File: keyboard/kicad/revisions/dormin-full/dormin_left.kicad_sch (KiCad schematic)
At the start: 104 parts, among them J6_R1 Conn_01x04, Q3_R1 AO3407A, Q4_R1 AO3400A, SW21 SW_Push, SW22 SW_Push, SW23 SW_Push, SW24 SW_Push, SW25 SW_Push, SW26 SW_Push, SW27 SW_Push, SW28 SW_Push, SW29 SW_Push, SW30 SW_Push, SW31 SW_Push, SW32 SW_Push, SW33 SW_Push, SW34 SW_Push, SW35 SW_Push, SW36 SW_Push, SW37 SW_Push, SW38 SW_Push, SW39 SW_Push, SW40 SW_Push, U2 Seeeduino Xiao nRF52840

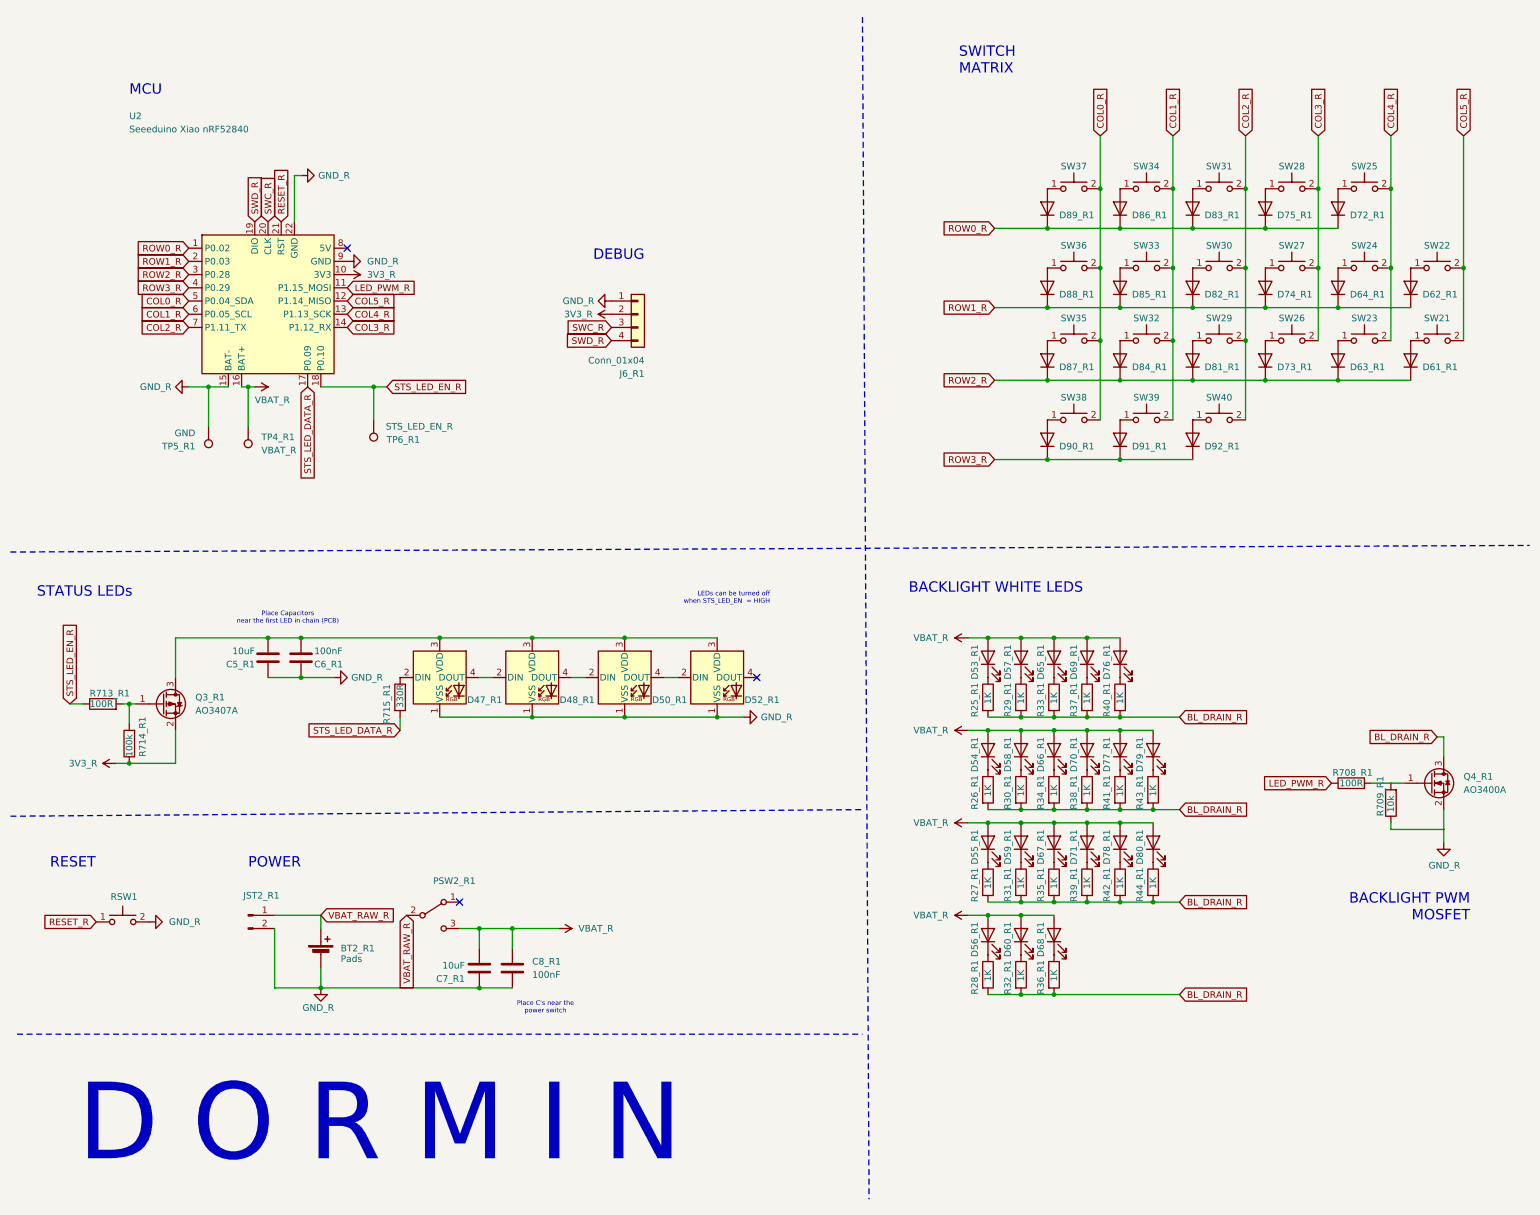
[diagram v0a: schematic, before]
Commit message: feat: remove unused components for v1
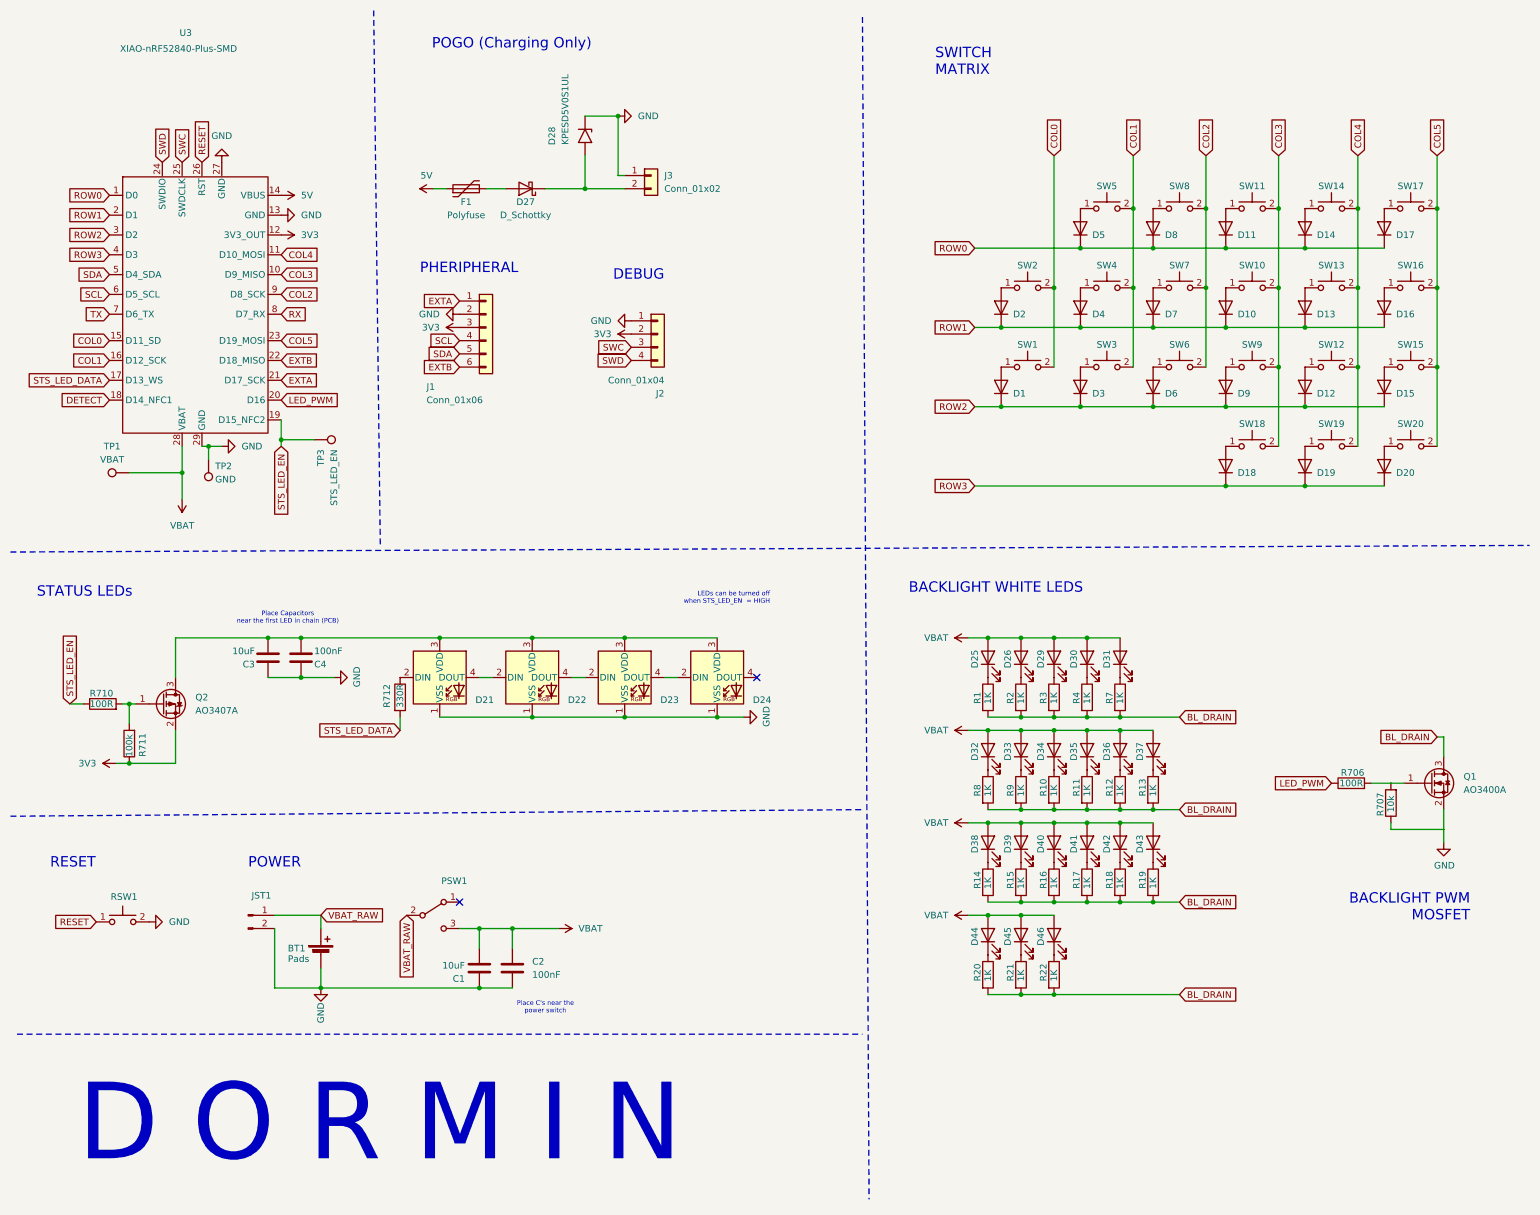
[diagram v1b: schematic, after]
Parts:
- removed BT2_R1: Pads, willkeebs_power:Battery_Pad, symbol Device:Battery_Cell
- removed C5_R1, C7_R1: 10uF, Capacitor_SMD:C_0603_1608Metric, symbol Device:C
- removed C6_R1, C8_R1: 100nF, Capacitor_SMD:C_0603_1608Metric, symbol Device:C
- removed D47_R1, D48_R1, D50_R1, D52_R1: SK6812MINI-E, LED_SMD:LED_SK6812MINI-E_3.2x2.8mm_P1.5mm_ReverseMount, symbol LED:SK6812MINI-E
- removed D53_R1, D54_R1, D55_R1, D56_R1, D57_R1, D58_R1, D59_R1, D60_R1, D65_R1, D66_R1, D67_R1, D68_R1, D69_R1, D70_R1, D71_R1, D76_R1, D77_R1, D78_R1, D79_R1, D80_R1: LED, willkeebs_components:LED_MHT151WDT, symbol Device:LED
- removed D61_R1, D62_R1, D63_R1, D64_R1, D72_R1, D73_R1, D74_R1, D75_R1, D81_R1, D82_R1, D83_R1, D84_R1, D85_R1, D86_R1, D87_R1, D88_R1, D89_R1, D90_R1, D91_R1, D92_R1: 1N4148W, Diode_SMD:D_SOD-123, symbol Diode:1N4148W
- removed J6_R1: Conn_01x04, Connector_PinSocket_2.54mm:PinSocket_1x04_P2.54mm_Vertical, symbol Connector_Generic:Conn_01x04
- removed JST2_R1: Conn_01x02_Pin, Connector_JST:JST_GH_SM02B-GHS-TB_1x02-1MP_P1.25mm_Horizontal, symbol Connector:Conn_01x02_Pin
- removed PSW2_R1: SW_SPDT, PCM_marbastlib-various:SW_MSK12C02-HB, symbol Switch:SW_SPDT
- removed Q3_R1: AO3407A, Package_TO_SOT_SMD:SOT-23, symbol Transistor_FET:AO3401A
- removed Q4_R1: AO3400A, Package_TO_SOT_SMD:SOT-23, symbol Transistor_FET:AO3400A
- removed R25_R1, R26_R1, R27_R1, R28_R1, R29_R1, R30_R1, R31_R1, R32_R1, R33_R1, R34_R1, R35_R1, R36_R1, R37_R1, R38_R1, R39_R1, R40_R1, R41_R1, R42_R1, R43_R1, R44_R1: 1K, Resistor_SMD:R_0603_1608Metric, symbol Device:R
- removed R708_R1, R713_R1: 100R, Resistor_SMD:R_0603_1608Metric, symbol Device:R
- removed R709_R1: 10k, Resistor_SMD:R_0603_1608Metric, symbol Device:R
- removed R714_R1: 100k, Resistor_SMD:R_0603_1608Metric, symbol Device:R
- removed R715_R1: 330R, Resistor_SMD:R_0603_1608Metric, symbol Device:R
- removed RSW2_R1: RSW1, Button_Switch_SMD:SW_SPST_SKQG_WithStem, symbol Switch:SW_Push
- removed SW21, SW22, SW23, SW24, SW25, SW26, SW27, SW28, SW29, SW30, SW31, SW32, SW33, SW34, SW35, SW36, SW37, SW38, SW39, SW40: SW_Push, willkeebs_keyboard:NF_LED_1206_SW_KS33_3_0_HS_1U, symbol Switch:SW_Push
- removed TP4_R1: VBAT_R, TestPoint:TestPoint_Pad_D1.0mm, symbol Connector:TestPoint
- removed TP5_R1: GND, TestPoint:TestPoint_Pad_D1.0mm, symbol Connector:TestPoint
- removed TP6_R1: STS_LED_EN_R, TestPoint:TestPoint_Pad_D1.0mm, symbol Connector:TestPoint
- removed U2: Seeeduino Xiao nRF52840, Seeed_Studio_XIAO_Series:XIAO-nRF52840-SMD, symbol PCM_marbastlib-promicroish:Seeeduino_Xiao_nRF52840
- added BT1: Pads, willkeebs_power:Battery_Pad, symbol Device:Battery_Cell
- added C1, C3: 10uF, Capacitor_SMD:C_0603_1608Metric, symbol Device:C
- added C2, C4: 100nF, Capacitor_SMD:C_0603_1608Metric, symbol Device:C
- added D1, D10, D11, D12, D13, D14, D15, D16, D17, D18, D19, D2, D20, D3, D4, D5, D6, D7, D8, D9: 1N4148W, Diode_SMD:D_SOD-123, symbol Diode:1N4148W
- added D21, D22, D23, D24: SK6812MINI-E, LED_SMD:LED_SK6812MINI-E_3.2x2.8mm_P1.5mm_ReverseMount, symbol LED:SK6812MINI-E
- added D25, D26, D29, D30, D31, D32, D33, D34, D35, D36, D37, D38, D39, D40, D41, D42, D43, D44, D45, D46: LED, willkeebs_components:LED_MHT151WDT, symbol Device:LED
- added D27: D_Schottky, Diode_SMD:D_SOD-523, symbol Device:D_Schottky
- added D28: KPESD5V0S1UL, Diode_SMD:D_SOD-882, symbol Diode:SMF5V0A
- added F1: Polyfuse, Fuse:Fuse_1206_3216Metric, symbol Device:Polyfuse
- added J1: Conn_01x06, willkeebs_misc:SMD_Conn_1x06_P2.54mm_Vertical, symbol Connector_Generic:Conn_01x06
- added J2: Conn_01x04, Connector_PinSocket_2.54mm:PinSocket_1x04_P2.54mm_Vertical, symbol Connector_Generic:Conn_01x04
- added J3: Conn_01x02, willkeebs_components:Pogo1x2-Right-Angle, symbol Connector_Generic:Conn_01x02
- added JST1: Conn_01x02_Pin, Connector_JST:JST_GH_SM02B-GHS-TB_1x02-1MP_P1.25mm_Horizontal, symbol Connector:Conn_01x02_Pin
- added PSW1: SW_SPDT, PCM_marbastlib-various:SW_MSK12C02-HB, symbol Switch:SW_SPDT
- added Q1: AO3400A, Package_TO_SOT_SMD:SOT-23, symbol Transistor_FET:AO3400A
- added Q2: AO3407A, Package_TO_SOT_SMD:SOT-23, symbol Transistor_FET:AO3401A
- added R1, R10, R11, R12, R13, R14, R15, R16, R17, R18, R19, R2, R20, R21, R22, R3, R4, R7, R8, R9: 1K, Resistor_SMD:R_0603_1608Metric, symbol Device:R
- added R706, R710: 100R, Resistor_SMD:R_0603_1608Metric, symbol Device:R
- added R707: 10k, Resistor_SMD:R_0603_1608Metric, symbol Device:R
- added R711: 100k, Resistor_SMD:R_0603_1608Metric, symbol Device:R
- added R712: 330R, Resistor_SMD:R_0603_1608Metric, symbol Device:R
- added RSW1: RSW1, Button_Switch_SMD:SW_SPST_SKQG_WithStem, symbol Switch:SW_Push
- added SW1, SW10, SW11, SW12, SW13, SW14, SW15, SW16, SW17, SW18, SW19, SW2, SW20, SW3, SW4, SW5, SW6, SW7, SW8, SW9: SW_Push, willkeebs_keyboard:NF_LED_1206_SW_KS33_3_0_HS_1U, symbol Switch:SW_Push
- added TP1: VBAT, TestPoint:TestPoint_Pad_D1.0mm, symbol Connector:TestPoint
- added TP2: GND, TestPoint:TestPoint_Pad_D1.0mm, symbol Connector:TestPoint
- added TP3: STS_LED_EN, TestPoint:TestPoint_Pad_D1.0mm, symbol Connector:TestPoint
- added U3: XIAO-nRF52840-Plus-SMD, Seeed_Studio_XIAO_Series:XIAO-nRF52840-Plus-SMD, symbol Seeed_Studio_XIAO_Series:XIAO-nRF52840_Plus_SMD
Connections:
- new net: D39.1 (K), R15.1
- new net: D32.1 (K), R8.1
- new net: D38.1 (K), R14.1
- new net: D20.2 (A), SW20.1
- new net: D43.1 (K), R19.1
- new net: D21.2 (DIN), R712.1
- new net: C3.2, C4.1, D21.3 (VDD), D22.3 (VDD), D23.3 (VDD), D24.3 (VDD), Q2.3 (D)
- new net: D2.2 (A), SW2.1
- new net: D19.2 (A), SW19.1
- new net: D35.1 (K), R11.1
- new net: D45.1 (K), R21.1
- new net: D9.2 (A), SW9.1
- new net: D14.2 (A), SW14.1
- new net: D33.1 (K), R9.1
- new net: D27.1 (K), D28.2 (A2), J3.2 (Pin_2)
- new net: D3.2 (A), SW3.1
- new net: D5.2 (A), SW5.1
- new net: D37.1 (K), R13.1
- new net: D4.2 (A), SW4.1
- new net: D11.2 (A), SW11.1
- new net: D13.2 (A), SW13.1
- new net: D12.2 (A), SW12.1
- new net: D31.1 (K), R7.1
- new net: D26.1 (K), R2.1
- new net: D6.2 (A), SW6.1
- new net: D27.2 (A), F1.2
- new net: D40.1 (K), R16.1
- new net: Q2.1 (G), R710.2, R711.2
- new net: D15.2 (A), SW15.1
- new net: D21.4 (DOUT), D22.2 (DIN)
- new net: D22.4 (DOUT), D23.2 (DIN)
- new net: D23.4 (DOUT), D24.2 (DIN)
- new net: D8.2 (A), SW8.1
- new net: D18.2 (A), SW18.1
- new net: D1.2 (A), SW1.1
- new net: D41.1 (K), R17.1
- new net: Q1.1 (G), R706.2, R707.2
- new net: D36.1 (K), R12.1
- new net: D42.1 (K), R18.1
- new net: D46.1 (K), R22.1
- new net: D44.1 (K), R20.1
- new net: D29.1 (K), R3.1
- new net: D30.1 (K), R4.1
- new net: D10.2 (A), SW10.1
- new net: D17.2 (A), SW17.1
- new net: D7.2 (A), SW7.1
- new net: D16.2 (A), SW16.1
- new net: D25.1 (K), R1.1
- new net: D34.1 (K), R10.1
- new net 3V3: J1.3 (Pin_3), J2.2 (Pin_2), Q2.2 (S), R711.1, U3.12 (3V3_OUT)
- new net 5V: F1.1, U3.14 (VBUS)
- new net BL_DRAIN: Q1.3 (D), R1.2, R10.2, R11.2, R12.2, R13.2, R14.2, R15.2, R16.2, R17.2, R18.2, R19.2, R2.2, R20.2, R21.2, R22.2, R3.2, R4.2, R7.2, R8.2, R9.2
- new net COL0: SW1.2, SW2.2, U3.15 (D11_SD)
- new net COL1: SW3.2, SW4.2, SW5.2, U3.16 (D12_SCK)
- new net COL2: SW6.2, SW7.2, SW8.2, U3.9 (D8_SCK)
- new net COL3: SW10.2, SW11.2, SW18.2, SW9.2, U3.10 (D9_MISO)
- new net COL4: SW12.2, SW13.2, SW14.2, SW19.2, U3.11 (D10_MOSI)
- new net COL5: SW15.2, SW16.2, SW17.2, SW20.2, U3.23 (D19_MOSI)
- new net DETECT: U3.18 (D14_NFC1)
- new net EXTA: J1.1 (Pin_1), U3.21 (D17_SCK)
- new net EXTB: J1.6 (Pin_6), U3.22 (D18_MISO)
- new net GND: BT1.2 (-), C1.2, C2.2, C3.1, C4.2, D21.1 (VSS), D22.1 (VSS), D23.1 (VSS), D24.1 (VSS), D28.1 (A1), J1.2 (Pin_2), J2.1 (Pin_1), J3.1 (Pin_1), JST1.2 (Pin_2), Q1.2 (S), R707.1, RSW1.2, TP2.1, U3.13 (GND), U3.27 (GND), U3.29 (GND)
- new net LED_PWM: R706.1, U3.20 (D16)
- new net RESET: RSW1.1, U3.26 (RST)
- new net ROW0: D11.1 (K), D14.1 (K), D17.1 (K), D5.1 (K), D8.1 (K), U3.1 (D0)
- new net ROW1: D10.1 (K), D13.1 (K), D16.1 (K), D2.1 (K), D4.1 (K), D7.1 (K), U3.2 (D1)
- new net ROW2: D1.1 (K), D12.1 (K), D15.1 (K), D3.1 (K), D6.1 (K), D9.1 (K), U3.3 (D2)
- new net ROW3: D18.1 (K), D19.1 (K), D20.1 (K), U3.4 (D3)
- new net RX: U3.8 (D7_RX)
- new net SCL: J1.4 (Pin_4), U3.6 (D5_SCL)
- new net SDA: J1.5 (Pin_5), U3.5 (D4_SDA)
- new net STS_LED_DATA: R712.2, U3.17 (D13_WS)
- new net STS_LED_EN: R710.1, TP3.1, U3.19 (D15_NFC2)
- new net SWC: J2.3 (Pin_3), U3.25 (SWDCLK)
- new net SWD: J2.4 (Pin_4), U3.24 (SWDIO)
- new net TX: U3.7 (D6_TX)
- new net VBAT: C1.1, C2.1, D25.2 (A), D26.2 (A), D29.2 (A), D30.2 (A), D31.2 (A), D32.2 (A), D33.2 (A), D34.2 (A), D35.2 (A), D36.2 (A), D37.2 (A), D38.2 (A), D39.2 (A), D40.2 (A), D41.2 (A), D42.2 (A), D43.2 (A), D44.2 (A), D45.2 (A), D46.2 (A), PSW1.3 (C), TP1.1, U3.28 (VBAT)
- new net VBAT_RAW: BT1.1 (+), JST1.1 (Pin_1), PSW1.2 (B)
- no-connect marks 3 -> 2
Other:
- note added: "PHERIPHERAL"
- note added: "POGO (Charging Only)"
- note removed: "MCU"
